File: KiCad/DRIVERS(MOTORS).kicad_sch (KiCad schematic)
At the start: 0 parts

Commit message: cambios en la parte de motors (aun incompleto debido a la falta de conexion con el microcontrolador
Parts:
- added C1, C2, C4, C6, C7, C9: 0.1uF, symbol Device:C
- added C3, C5, C8: 10uF, symbol Device:C
- added M1, M2, M3: Motor_DC, symbol Motor:Motor_DC
- added U1, U2, U3: TB6612FNG, Package_SO:SSOP-24_5.3x8.2mm_P0.65mm, symbol Driver_Motor:TB6612FNG
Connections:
- new net: M2.1 (+), U2.1 (AO1), U2.2 (AO1)
- new net: M2.2 (-), U2.5 (AO2), U2.6 (AO2)
- new net: M1.1 (+), U1.1 (AO1), U1.2 (AO1)
- new net: M1.2 (-), U1.5 (AO2), U1.6 (AO2)
- new net: M3.1 (+), U3.1 (AO1), U3.2 (AO1)
- new net: M3.2 (-), U3.5 (AO2), U3.6 (AO2)
- new net: U2.11 (BO1), U2.12 (BO1)
- new net: U2.7 (BO2), U2.8 (BO2)
- new net: U1.11 (BO1), U1.12 (BO1)
- new net: U1.7 (BO2), U1.8 (BO2)
- new net: U3.11 (BO1), U3.12 (BO1)
- new net: U3.7 (BO2), U3.8 (BO2)
- new net +12V: C2.1, C3.1, C5.1, C6.1, C8.1, C9.1, U1.13 (VM2), U1.14 (VM3), U1.24 (VM1), U2.13 (VM2), U2.14 (VM3), U2.24 (VM1), U3.13 (VM2), U3.14 (VM3), U3.24 (VM1)
- new net +5V: C1.1, C4.1, C7.1, U1.19 (STBY), U1.20 (VCC), U2.19 (STBY), U2.20 (VCC), U3.19 (STBY), U3.20 (VCC)
- new net ALT_IN1: U3.21 (AIN1)
- new net ALT_IN2: U3.22 (AIN2)
- new net ALT_PWM: U3.23 (PWMA)
- new net GND: C1.2, C2.2, C3.2, C4.2, C5.2, C6.2, C7.2, C8.2, C9.2, U1.10 (PGND2), U1.18 (GND), U1.3 (PGND1), U1.4 (PGND1), U1.9 (PGND2), U2.10 (PGND2), U2.18 (GND), U2.3 (PGND1), U2.4 (PGND1), U2.9 (PGND2), U3.10 (PGND2), U3.18 (GND), U3.3 (PGND1), U3.4 (PGND1), U3.9 (PGND2)
- new net POS_IN1: U1.21 (AIN1)
- new net POS_IN2: U1.22 (AIN2)
- new net POS_PWM: U1.23 (PWMA)
- new net REC_IN1: U2.21 (AIN1)
- new net REC_IN2: U2.22 (AIN2)
- new net REC_PWM: U2.23 (PWMA)
- no-connect marks 0 -> 15

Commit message: mamaguebo
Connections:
- net +5V renamed +3.3V

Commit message: Modificació
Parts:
- renumbered C1 to C10, C7 to C11, C3 to C12, C2 to C13, C8 to C14, C9 to C15, C4 to C16, C5 to C17, C6 to C18, M3 to M2, M2 to M3, U1 to U7, U3 to U8, U2 to U9
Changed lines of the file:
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@@
 		)
 		(property "Intersheetrefs" "${INTERSHEET_REFS}"
-			(at 33.5424 67.31 0)
+			(at 34.1966 67.31 0)
 			(effects
 				(font
@@
 		(dnp no)
 		(fields_autoplaced yes)
-		(property "Reference" "C?"
+		(property "Reference" "C17"
 			(at 271.78 87.6299 0)
 			(effects
@@
 			(project "SEIENTS_EDD"
 				(path "/b6401b4f-5426-49b8-bb2e-8ecdb19989ef/91c89211-2801-4487-b613-213c9c9ba611"
-					(reference "C?")
+					(reference "C17")
 					(unit 1)
 				)
@@
 		(dnp no)
 		(fields_autoplaced yes)
-		(property "Reference" "M?"
+		(property "Reference" "M3"
 			(at 264.16 46.9899 0)
 			(effects
@@
 			(project "SEIENTS_EDD"
 				(path "/b6401b4f-5426-49b8-bb2e-8ecdb19989ef/91c89211-2801-4487-b613-213c9c9ba611"
-					(reference "M?")
+					(reference "M3")
 					(unit 1)
 				)
@@
 		(dnp no)
 		(fields_autoplaced yes)
-		(property "Reference" "M?"
+		(property "Reference" "M1"
 			(at 105.41 58.4199 0)
 			(effects
@@
 			(project "SEIENTS_EDD"
 				(path "/b6401b4f-5426-49b8-bb2e-8ecdb19989ef/91c89211-2801-4487-b613-213c9c9ba611"
-					(reference "M?")
+					(reference "M1")
 					(unit 1)
 				)
@@
 		(dnp no)
 		(fields_autoplaced yes)
-		(property "Reference" "#FLG?"
+		(property "Reference" "#FLG0106"
 			(at 73.025 97.79 0)
 			(effects
@@
 			(project "SEIENTS_EDD"
 				(path "/b6401b4f-5426-49b8-bb2e-8ecdb19989ef/91c89211-2801-4487-b613-213c9c9ba611"
-					(reference "#FLG?")
+					(reference "#FLG0106")
 					(unit 1)
 				)
@@
 		(dnp no)
 		(fields_autoplaced yes)
-		(property "Reference" "#PWR?"
+		(property "Reference" "#PWR0107"
 			(at 87.63 190.5 0)
 			(effects
@@
 			(project "SEIENTS_EDD"
 				(path "/b6401b4f-5426-49b8-bb2e-8ecdb19989ef/91c89211-2801-4487-b613-213c9c9ba611"
-					(reference "#PWR?")
+					(reference "#PWR0107")
 					(unit 1)
 				)
@@
 		(dnp no)
 		(fields_autoplaced yes)
-		(property "Reference" "C?"
+		(property "Reference" "C12"
 			(at 113.03 99.0599 0)
 			(effects
@@
 			(project "SEIENTS_EDD"
 				(path "/b6401b4f-5426-49b8-bb2e-8ecdb19989ef/91c89211-2801-4487-b613-213c9c9ba611"
-					(reference "C?")
+					(reference "C12")
 					(unit 1)
 				)
@@
 		(dnp no)
 		(fields_autoplaced yes)
-		(property "Reference" "#FLG?"
+		(property "Reference" "#FLG0107"
 			(at 44.45 37.465 0)
 			(effects
@@
 			(project "SEIENTS_EDD"
 				(path "/b6401b4f-5426-49b8-bb2e-8ecdb19989ef/91c89211-2801-4487-b613-213c9c9ba611"
-					(reference "#FLG?")
+					(reference "#FLG0107")
 					(unit 1)
 				)
@@
 		(dnp no)
 		(fields_autoplaced yes)
-		(property "Reference" "C?"
+		(property "Reference" "C18"
 			(at 278.13 77.4699 0)
 			(effects
@@
 			(project "SEIENTS_EDD"
 				(path "/b6401b4f-5426-49b8-bb2e-8ecdb19989ef/91c89211-2801-4487-b613-213c9c9ba611"
-					(reference "C?")
+					(reference "C18")
 					(unit 1)
 				)
@@
 		(dnp no)
 		(fields_autoplaced yes)
-		(property "Reference" "#PWR?"
+		(property "Reference" "#PWR0105"
 			(at 233.68 93.98 0)
 			(effects
@@
 			(project "SEIENTS_EDD"
 				(path "/b6401b4f-5426-49b8-bb2e-8ecdb19989ef/91c89211-2801-4487-b613-213c9c9ba611"
-					(reference "#PWR?")
+					(reference "#PWR0105")
 					(unit 1)
 				)
@@
 		(dnp no)
 		(fields_autoplaced yes)
-		(property "Reference" "#PWR?"
+		(property "Reference" "#PWR0106"
 			(at 46.99 39.37 0)
 			(effects
@@
 			(project "SEIENTS_EDD"
 				(path "/b6401b4f-5426-49b8-bb2e-8ecdb19989ef/91c89211-2801-4487-b613-213c9c9ba611"
-					(reference "#PWR?")
+					(reference "#PWR0106")
 					(unit 1)
 				)
@@
 		(dnp no)
 		(fields_autoplaced yes)
-		(property "Reference" "M?"
+		(property "Reference" "M2"
 			(at 118.11 143.5099 0)
 			(effects
@@
 			(project "SEIENTS_EDD"
 				(path "/b6401b4f-5426-49b8-bb2e-8ecdb19989ef/91c89211-2801-4487-b613-213c9c9ba611"
-					(reference "M?")
+					(reference "M2")
 					(unit 1)
 				)
@@
 		(dnp no)
 		(fields_autoplaced yes)
-		(property "Reference" "C?"
+		(property "Reference" "C11"
 			(at 58.42 170.1799 0)
 			(effects
@@
 			(project "SEIENTS_EDD"
 				(path "/b6401b4f-5426-49b8-bb2e-8ecdb19989ef/91c89211-2801-4487-b613-213c9c9ba611"
-					(reference "C?")
+					(reference "C11")
 					(unit 1)
 				)
@@
 		(dnp no)
 		(fields_autoplaced yes)
-		(property "Reference" "C?"
+		(property "Reference" "C16"
 			(at 204.47 73.6599 0)
 			(effects
@@
 			(project "SEIENTS_EDD"
 				(path "/b6401b4f-5426-49b8-bb2e-8ecdb19989ef/91c89211-2801-4487-b613-213c9c9ba611"
-					(reference "C?")
+					(reference "C16")
 					(unit 1)
 				)
@@
 		(dnp no)
 		(fields_autoplaced yes)
-		(property "Reference" "U?"
+		(property "Reference" "U9"
 			(at 240.9033 76.2 0)
 			(effects
@@
 			(project "SEIENTS_EDD"
 				(path "/b6401b4f-5426-49b8-bb2e-8ecdb19989ef/91c89211-2801-4487-b613-213c9c9ba611"
-					(reference "U?")
+					(reference "U9")
 					(unit 1)
 				)
@@
 		(dnp no)
 		(fields_autoplaced yes)
-		(property "Reference" "#PWR?"
+		(property "Reference" "#PWR0104"
 			(at 74.93 105.41 0)
 			(effects
@@
 			(project "SEIENTS_EDD"
 				(path "/b6401b4f-5426-49b8-bb2e-8ecdb19989ef/91c89211-2801-4487-b613-213c9c9ba611"
-					(reference "#PWR?")
+					(reference "#PWR0104")
 					(unit 1)
 				)
@@
 		(dnp no)
 		(fields_autoplaced yes)
-		(property "Reference" "U?"
+		(property "Reference" "U7"
 			(at 82.1533 87.63 0)
 			(effects
@@
 			(project "SEIENTS_EDD"
 				(path "/b6401b4f-5426-49b8-bb2e-8ecdb19989ef/91c89211-2801-4487-b613-213c9c9ba611"
-					(reference "U?")
+					(reference "U7")
 					(unit 1)
 				)
@@
 		(dnp no)
 		(fields_autoplaced yes)
-		(property "Reference" "C?"
+		(property "Reference" "C14"
 			(at 125.73 184.1499 0)
 			(effects
@@
 			(project "SEIENTS_EDD"
 				(path "/b6401b4f-5426-49b8-bb2e-8ecdb19989ef/91c89211-2801-4487-b613-213c9c9ba611"
-					(reference "C?")
+					(reference "C14")
 					(unit 1)
 				)
@@
 		(dnp no)
 		(fields_autoplaced yes)
-		(property "Reference" "C?"
+		(property "Reference" "C13"
 			(at 119.38 88.8999 0)
 			(effects
@@
 			(project "SEIENTS_EDD"
 				(path "/b6401b4f-5426-49b8-bb2e-8ecdb19989ef/91c89211-2801-4487-b613-213c9c9ba611"
-					(reference "C?")
+					(reference "C13")
 					(unit 1)
 				)
@@
 		(dnp no)
 		(fields_autoplaced yes)
-		(property "Reference" "U?"
+		(property "Reference" "U8"
 			(at 94.8533 172.72 0)
 			(effects
@@
 			(project "SEIENTS_EDD"
 				(path "/b6401b4f-5426-49b8-bb2e-8ecdb19989ef/91c89211-2801-4487-b613-213c9c9ba611"
-					(reference "U?")
+					(reference "U8")
 					(unit 1)
 				)
@@
 		(dnp no)
 		(fields_autoplaced yes)
-		(property "Reference" "C?"
+		(property "Reference" "C15"
 			(at 132.08 173.9899 0)
 			(effects
@@
 			(project "SEIENTS_EDD"
 				(path "/b6401b4f-5426-49b8-bb2e-8ecdb19989ef/91c89211-2801-4487-b613-213c9c9ba611"
-					(reference "C?")
+					(reference "C15")
 					(unit 1)
 				)
@@
 		(dnp no)
 		(fields_autoplaced yes)
-		(property "Reference" "C?"
+		(property "Reference" "C10"
 			(at 45.72 85.0899 0)
 			(effects
@@
 			(project "SEIENTS_EDD"
 				(path "/b6401b4f-5426-49b8-bb2e-8ecdb19989ef/91c89211-2801-4487-b613-213c9c9ba611"
-					(reference "C?")
-					(unit 1)
-				)
+					(reference "C10")
+					(unit 1)
+				)

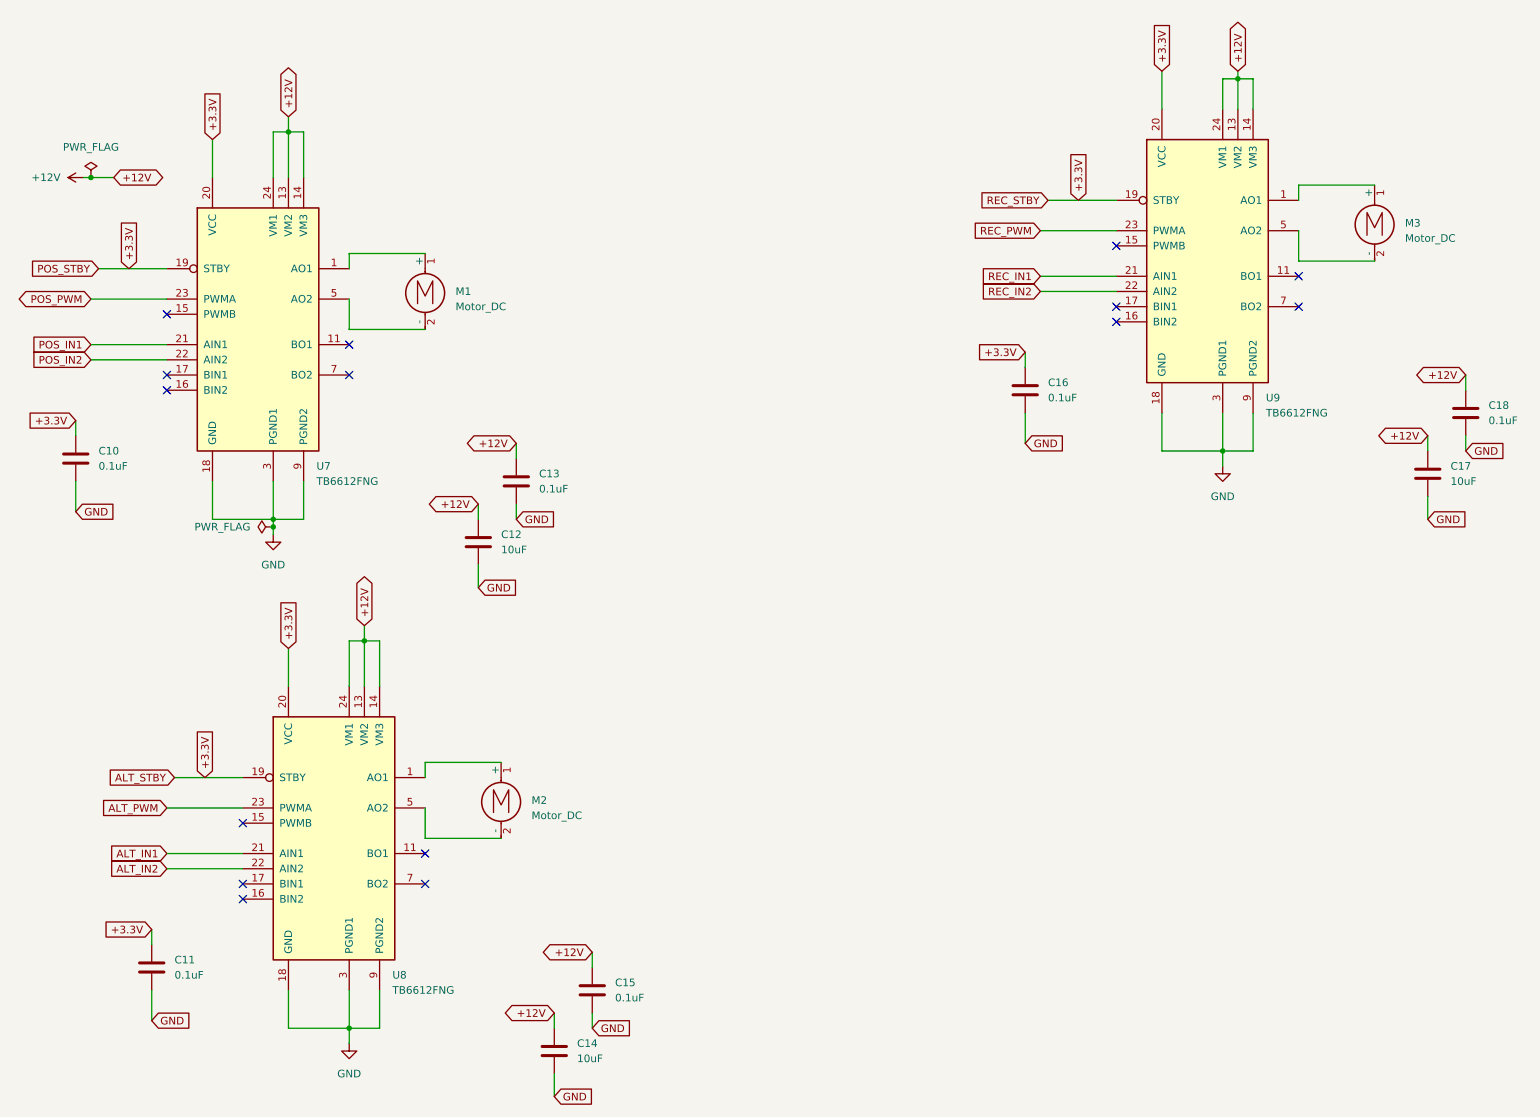
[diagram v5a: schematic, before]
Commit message: Cambios en motors (etiqetas)
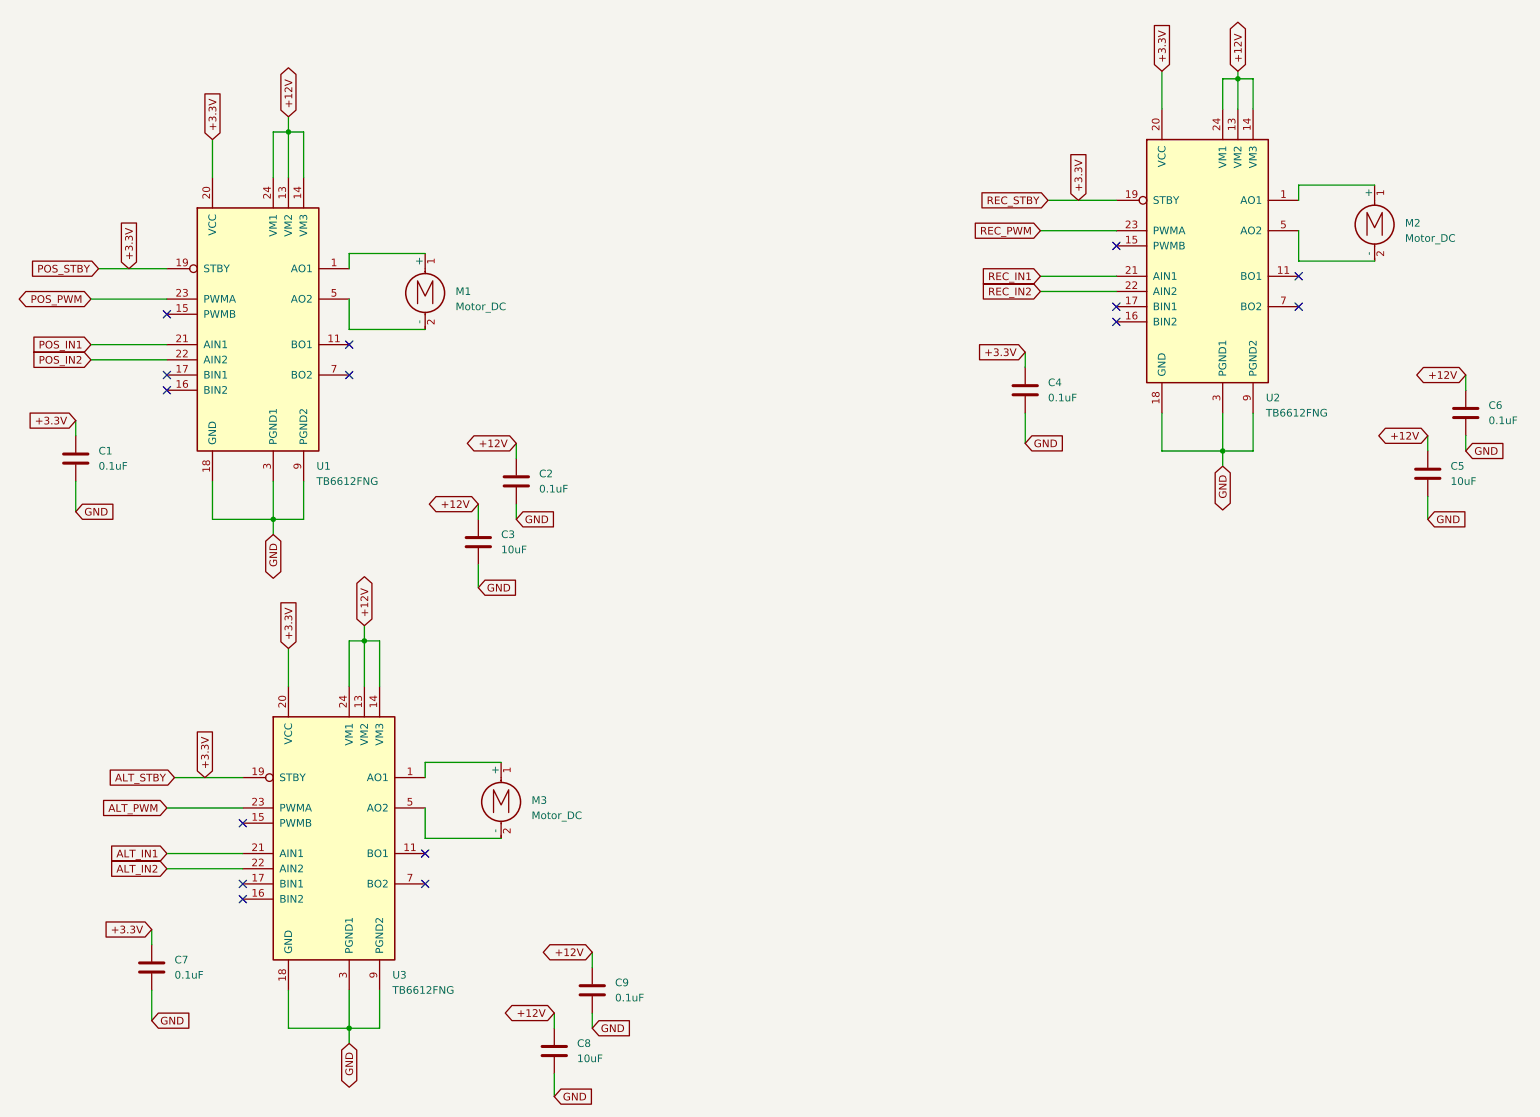
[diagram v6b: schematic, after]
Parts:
- renumbered C10 to C1, C13 to C2, C12 to C3, C16 to C4, C17 to C5, C18 to C6, C11 to C7, C14 to C8, C15 to C9, M3 to M2, M2 to M3, U7 to U1, U9 to U2, U8 to U3

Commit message: Canvis al KICAD
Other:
- moved on the sheet: C1, C2, C3, C4, C5, C6, C7, C8, C9, M1, M2, M3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
